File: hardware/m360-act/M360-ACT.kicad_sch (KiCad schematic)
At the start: 59 parts, among them J1 5V do quadro, J2 M360-RF, J3 RJ45 RELES-A, J4 RJ45 RELES-B, J5 RJ45 SENSORES, Q1 AO3401A, SW1 Reed, U1 ME6211C33M5, U2 74HCT244, U3 CD74HC4067, U4 SRV05-4, U5 SRV05-4, U6 SRV05-4, U7 SRV05-4, U8 SRV05-4

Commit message: fix(hardware): ACT — canais dos TVS pela ordem física dos pinos do RJ45
- esquemático: 8 labels trocados nos pinos de U4-U7 (REL_CH0/CH4, CH2/CH5,
  CH6/CH8, CH9/OXI), para as pernas RJ45 -> TVS saírem sem cruzar (§11.8);
  netdiff só nos 8 pinos, ERC 0, campos e lib_symbols idênticos
- §5.2: mapeamento, ordem de saída adotada (pino 5 contorna sob a pega, como
  o SOIL2 da LP) e o que a placa precisa (par de TVS a 180° por RJ45, U3 e
  R21-R32 ordenados pela saída dos TVS)
- leque_tvs.py: VP em qualquer rede (+5V na ACT) e nada de cobre em canal sem uso
- ordem_tvs.py: preset act
- datasheet do SRV05-4 TECH PUBLIC (C558418): pinos 1/3/4/6 = I/O equivalentes
- correções da revisão adversarial da troca

Co-Authored-By: Claude Opus 5 (1M context) <noreply@anthropic.com>
Claude-Session: https://claude.ai/code/session_012t7RkcrXvvpDVjKVimNu18
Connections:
- net REL_CH0: now also U5.1 (IO1); no longer U4.1 (IO1)
- net REL_CH2: now also U5.3 (IO2); no longer U4.4 (IO3)
- net REL_CH4: now also U4.1 (IO1); no longer U5.1 (IO1)
- net REL_CH5: now also U4.4 (IO3); no longer U5.3 (IO2)
- net REL_CH6: now also U7.1 (IO1); no longer U6.1 (IO1)
- net REL_CH8: now also U6.1 (IO1); no longer U7.1 (IO1)
- net REL_CH9: now also U6.4 (IO3); no longer U7.3 (IO2)
- net REL_OXI: now also U7.3 (IO2); no longer U6.4 (IO3)
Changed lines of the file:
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@@
 		)
 	)
-	(label "REL_CH9"
+	(label "REL_OXI"
 		(at 292.1 182.88 0)
 		(effects
@@
 		)
 	)
-	(label "REL_CH2"
+	(label "REL_CH5"
 		(at 337.82 46.99 180)
 		(effects
@@
 		)
 	)
-	(label "REL_CH5"
+	(label "REL_CH2"
 		(at 292.1 92.71 0)
 		(effects
@@
 		)
 	)
-	(label "REL_CH8"
+	(label "REL_CH6"
 		(at 292.1 177.8 0)
 		(effects
@@
 		)
 	)
-	(label "REL_CH4"
+	(label "REL_CH0"
 		(at 292.1 87.63 0)
 		(effects
@@
 		)
 	)
-	(label "REL_CH6"
+	(label "REL_CH8"
 		(at 292.1 137.16 0)
 		(effects
@@
 		)
 	)
-	(label "REL_OXI"
+	(label "REL_CH9"
 		(at 337.82 137.16 180)
 		(effects
@@
 		)
 	)
-	(label "REL_CH0"
+	(label "REL_CH4"
 		(at 292.1 46.99 0)
 		(effects

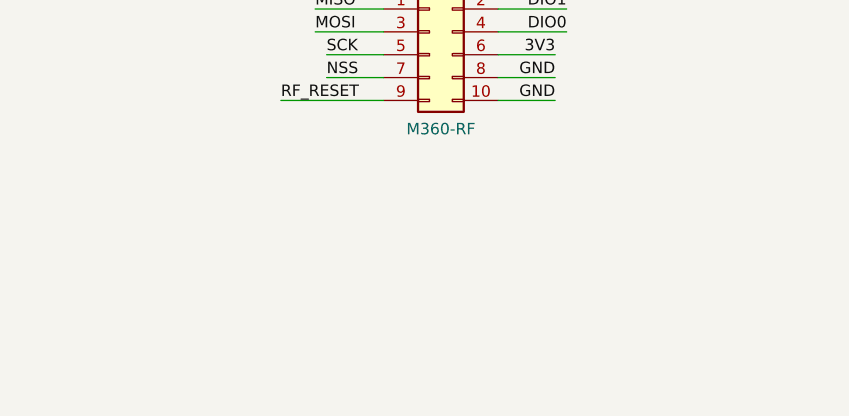
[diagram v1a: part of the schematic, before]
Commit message: feat(hardware): header 1x8 do nRF24 legado nas placas GW, LP e ACT
- esquemáticos: header 1x8 "nRF24 legado" (GW J4, LP J5, ACT J6; C492407,
  solda manual, fora do BOM e da posição) e 10 uF 0805 (C5/C16/C9, C15850)
  nas mesmas redes do soquete do mezanino: CE = DIO0, CSN = NSS, IRQ = DIO1
  (sem ligação na GW). Um rádio por placa: nRF24 OU mezanino RFM95W
- tools/add_nrf_header.py: grava símbolo, fios e labels por texto, embute o
  Conn_01x08 stock e confere colisão; netdiff só nas redes previstas, ERC 0,
  campos e lib_symbols inalterados nas três folhas
- placas rerroteadas sem apagar a fiação existente (DSN com fios fixos e
  cobertos por área proibida, mais áreas proibidas sobre os fiduciais);
  vias de GND junto do pino 8 e do capacitor; legenda "nRF24 OU mezanino"
  e "CE" no pino 1. GW 287 trilhas/43 vias, LP 855/135, ACT 939/141;
  DRC --severity-all 0/0, paridade idêntica, ordem_tvs 13/13 e 15/15
- fabricacao/ regerada: GW 15, LP 53, ACT 54 peças
- ARQUITETURA §2 (decisão 15), §4.2, §5.2, §6.1, §8, §9, §9.1; datasheet
  C492407 em docs/datasheets. Firmware pendente: MY_RF24_CE_PIN=5 (GW) e
  =2 (LP/ACT), a testar na bancada

Co-Authored-By: Claude Fable 5.1 <noreply@anthropic.com>
Claude-Session: https://claude.ai/code/session_01M8U92DFNnZt7SqLtzrKYSR
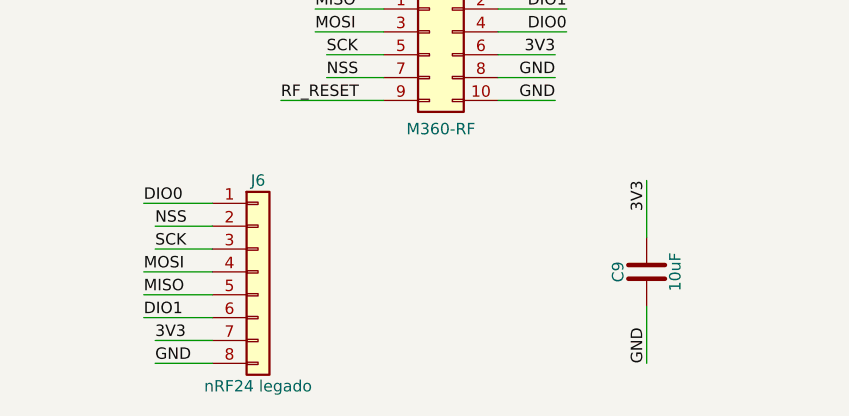
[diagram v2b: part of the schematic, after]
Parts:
- added C9: 10uF, Capacitor_SMD:C_0805_2012Metric, symbol Device:C
- added J6: nRF24 legado, Connector_PinHeader_2.54mm:PinHeader_1x08_P2.54mm_Vertical, symbol Connector_Generic:Conn_01x08
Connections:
- net 3V3: now also C9.1, J6.7 (Pin_7)
- net DIO0: now also J6.1 (Pin_1)
- net DIO1: now also J6.6 (Pin_6)
- net GND: now also C9.2, J6.8 (Pin_8)
- net MISO: now also J6.5 (Pin_5)
- net MOSI: now also J6.4 (Pin_4)
- net NSS: now also J6.2 (Pin_2)
- net SCK: now also J6.3 (Pin_3)
